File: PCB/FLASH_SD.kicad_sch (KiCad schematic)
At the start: 36 parts, among them J501 MEM2090-00-145-00-A_REVA, U1 IS21ES08GA-JQLI-TR, U502 HSP051-4M10, U503 HSP051-4M10

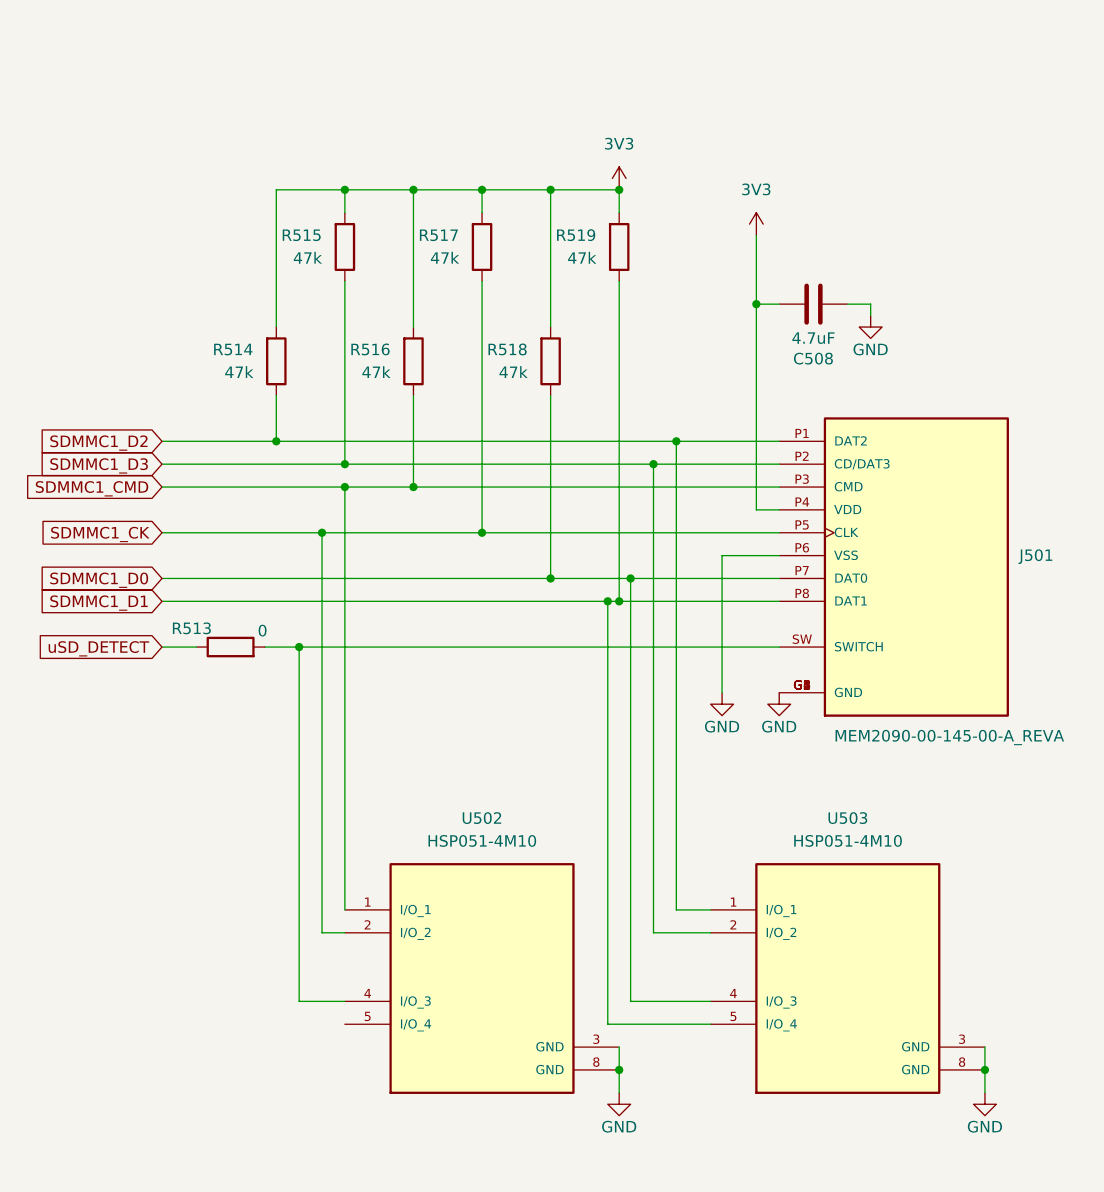
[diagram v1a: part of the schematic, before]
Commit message: PCB_UPDATE SD CARD DONE
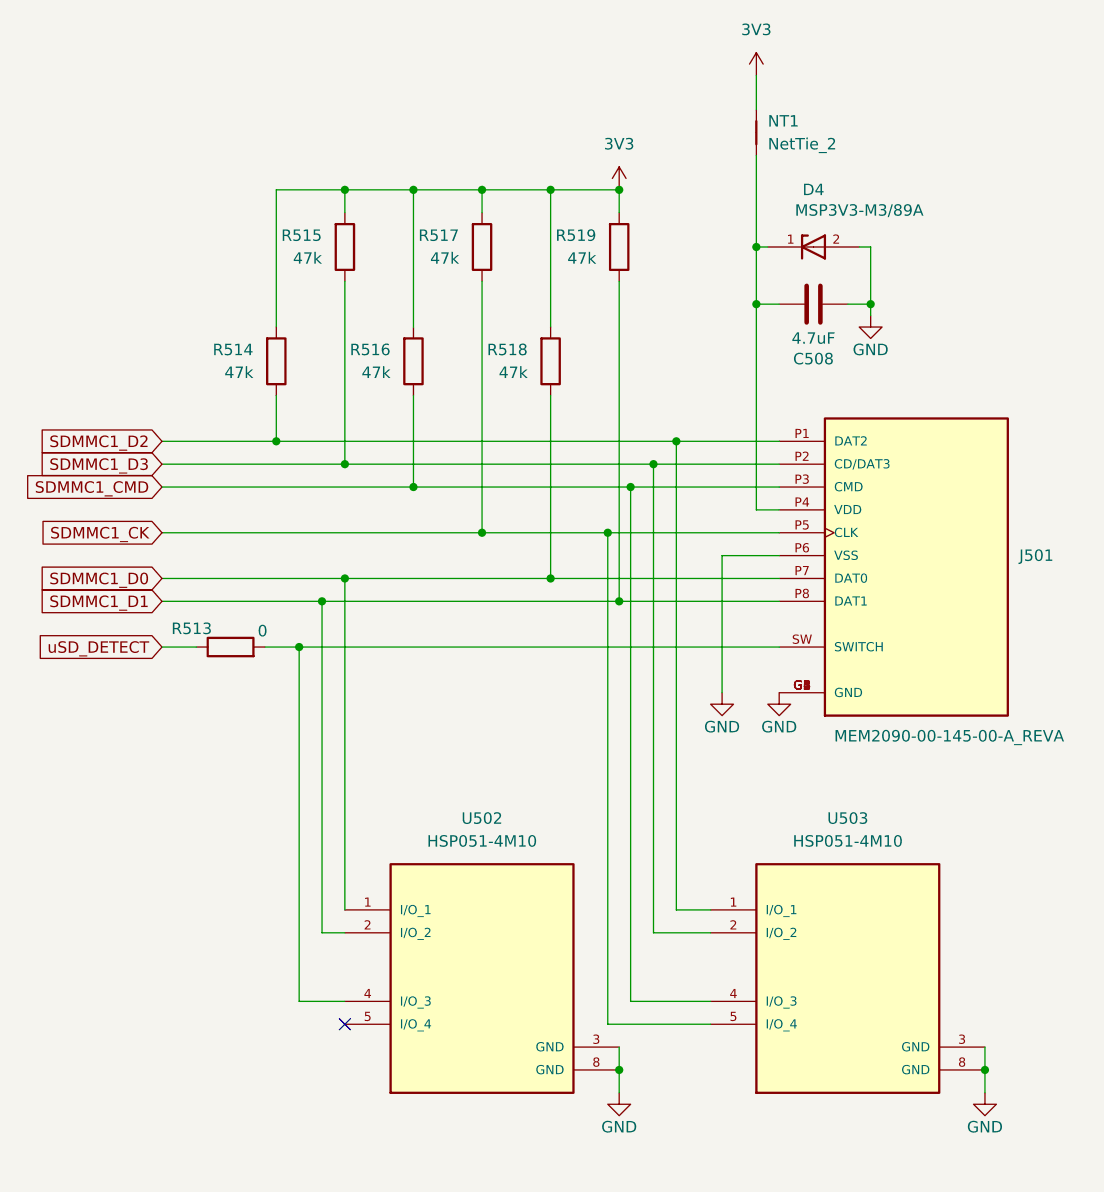
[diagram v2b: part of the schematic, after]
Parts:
- added D4: MSP3V3-M3/89A, Diode_SMD:D_MicroSMP_KA, symbol PTVS3V3S1UR:PTVS3V3S1UR
- added NT1: NetTie_2, NetTie:NetTie-2_SMD_Pad0.5mm, symbol Device:NetTie_2
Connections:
- net 3V3: now also NT1.2; no longer C508.2, J501.P4 (VDD)
- net GND: now also D4.2
- net SDMMC1_CK: now also U503.5 (I/O_4), U503.6 (NC); no longer U502.2 (I/O_2), U502.9 (NC)
- net SDMMC1_CMD: now also U503.4 (I/O_3), U503.7 (NC); no longer U502.1 (I/O_1), U502.10 (NC)
- net SDMMC1_D0: now also U502.1 (I/O_1), U502.10 (NC); no longer U503.4 (I/O_3), U503.7 (NC)
- net SDMMC1_D1: now also U502.2 (I/O_2), U502.9 (NC); no longer U503.5 (I/O_4), U503.6 (NC)
- new net: C508.2, D4.1, J501.P4 (VDD), NT1.1
- no-connect marks 1 -> 2
